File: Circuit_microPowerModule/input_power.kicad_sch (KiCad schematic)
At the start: 42 parts, among them Q2 MMBT3906, Q3 IRF5305S, Q4 RK7002BM, SW4 SW_SPDT, U7 MP2315S

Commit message: change licenses
updated some footprint, create nokia 5110 lcd module pcb symbol, updated reademe
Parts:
- D4: footprint (none) -> LED_SMD:LED_1206_3216Metric
- Q4: footprint (none) -> Package_TO_SOT_SMD:SOT-23-3
- R19, R20, R21, R22, R23, R24, R25, R26, R27, R28, R29, R30, R59, R60: footprint (none) -> Resistor_SMD:R_0603_1608Metric
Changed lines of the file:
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@@
       (effects (font (size 1.27 1.27)) (justify left))
     )
-    (property "Footprint" "" (at 241.3 43.434 0)
+    (property "Footprint" "Resistor_SMD:R_0603_1608Metric" (at 241.3 43.434 0)
       (effects (font (size 1.27 1.27)) hide)
     )
@@
       (effects (font (size 1.27 1.27)) (justify left))
     )
-    (property "Footprint" "" (at 68.58 43.434 0)
+    (property "Footprint" "Resistor_SMD:R_0603_1608Metric" (at 68.58 43.434 0)
       (effects (font (size 1.27 1.27)) hide)
     )
@@
       (effects (font (size 2.54 2.54) bold (color 255 0 0 1)) (justify left))
     )
-    (property "Footprint" "" (at 91.44 58.166 0)
+    (property "Footprint" "Resistor_SMD:R_0603_1608Metric" (at 91.44 58.166 0)
       (effects (font (size 1.27 1.27)) hide)
     )
@@
       (effects (font (size 1.27 1.27)))
     )
-    (property "Footprint" "" (at 205.232 66.04 0)
+    (property "Footprint" "Resistor_SMD:R_0603_1608Metric" (at 205.232 66.04 0)
       (effects (font (size 1.27 1.27)) hide)
     )
@@
       (effects (font (size 1.27 1.27)) (justify left))
     )
-    (property "Footprint" "" (at 144.78 43.18 0)
+    (property "Footprint" "Resistor_SMD:R_0603_1608Metric" (at 144.78 43.18 0)
       (effects (font (size 1.27 1.27)) hide)
     )
@@
       (effects (font (size 1.27 1.27)) (justify left))
     )
-    (property "Footprint" "" (at 144.78 67.818 0)
+    (property "Footprint" "Resistor_SMD:R_0603_1608Metric" (at 144.78 67.818 0)
       (effects (font (size 1.27 1.27)) hide)
     )
@@
       (effects (font (size 1.27 1.27)) (justify left))
     )
-    (property "Footprint" "" (at 116.84 70.104 0)
+    (property "Footprint" "Resistor_SMD:R_0603_1608Metric" (at 116.84 70.104 0)
       (effects (font (size 1.27 1.27)) hide)
     )
@@
       (effects (font (size 1.27 1.27)))
     )
-    (property "Footprint" "" (at 186.182 66.04 0)
+    (property "Footprint" "Resistor_SMD:R_0603_1608Metric" (at 186.182 66.04 0)
       (effects (font (size 1.27 1.27)) hide)
     )
@@
       (effects (font (size 1.27 1.27)) (justify left))
     )
-    (property "Footprint" "" (at 38.1 133.35 0)
+    (property "Footprint" "Resistor_SMD:R_0603_1608Metric" (at 38.1 133.35 0)
       (effects (font (size 1.27 1.27)) hide)
     )
@@
       (effects (font (size 1.27 1.27)))
     )
-    (property "Footprint" "" (at 172.72 68.58 0)
+    (property "Footprint" "Package_TO_SOT_SMD:SOT-23-3" (at 172.72 68.58 0)
       (effects (font (size 1.27 1.27)) hide)
     )
@@
       (effects (font (size 1.27 1.27)))
     )
-    (property "Footprint" "" (at 99.314 51.308 0)
+    (property "Footprint" "Resistor_SMD:R_0603_1608Metric" (at 99.314 51.308 0)
       (effects (font (size 1.27 1.27)) hide)
     )
@@
       (effects (font (size 1.27 1.27)) (justify left))
     )
-    (property "Footprint" "" (at 170.18 45.72 0)
+    (property "Footprint" "Resistor_SMD:R_0603_1608Metric" (at 170.18 45.72 0)
       (effects (font (size 1.27 1.27)) hide)
     )
@@
       (effects (font (size 1.27 1.27)) (justify left))
     )
-    (property "Footprint" "" (at 38.1 123.19 0)
+    (property "Footprint" "Resistor_SMD:R_0603_1608Metric" (at 38.1 123.19 0)
       (effects (font (size 1.27 1.27)) hide)
     )
@@
       (effects (font (size 1.27 1.27)) (justify right))
     )
-    (property "Footprint" "" (at 158.75 70.358 0)
+    (property "Footprint" "Resistor_SMD:R_0603_1608Metric" (at 158.75 70.358 0)
       (effects (font (size 1.27 1.27)) hide)
     )
@@
       (effects (font (size 1.27 1.27)) (justify left))
     )
-    (property "Footprint" "" (at 195.58 45.72 0)
+    (property "Footprint" "Resistor_SMD:R_0603_1608Metric" (at 195.58 45.72 0)
       (effects (font (size 1.27 1.27)) hide)
     )
@@
       (effects (font (size 1.27 1.27)) (justify right))
     )
-    (property "Footprint" "" (at 241.3 52.832 90)
-      (effects (font (size 1.27 1.27)) hide)
-    )
+    (property "Footprint" "LED_SMD:LED_1206_3216Metric" (at 241.3 52.832 90)
+      (effects (font (size 1.27 1.27)) hide)
+    )

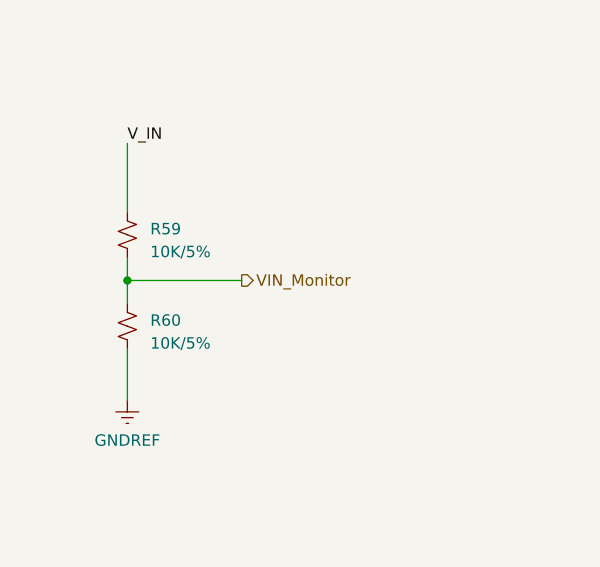
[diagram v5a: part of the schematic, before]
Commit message: update components footprint
check boost VR component, added Nokia 5110 LCD 3D module
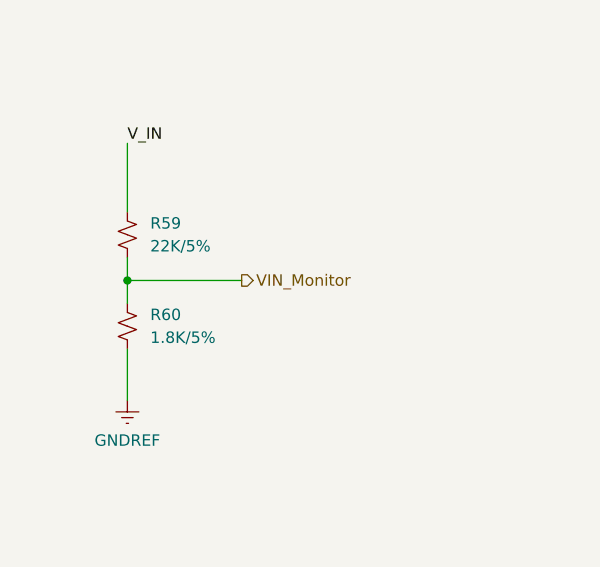
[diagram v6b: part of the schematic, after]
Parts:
- C1, C10, C11, C14, C2, C3, C6: footprint (none) -> Capacitor_SMD:C_0603_1608Metric
- D2, D3: footprint (none) -> Diode_SMD:D_SOD-123
- L1: footprint (none) -> Inductor_SMD_Wurth:L_Wurth_WE-LQSH-2512
- R59: value 10K/5% -> 22K/5%
- R60: value 10K/5% -> 1.8K/5%
- SW4: footprint (none) -> Button_Switch_THT:SW_Push_2P2T_Toggle_CK_PVA2xxH1xxxxxxV2
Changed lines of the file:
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@@
       (effects (font (size 1.27 1.27)) (justify left))
     )
-    (property "Footprint" "" (at 123.063 110.617 0)
+    (property "Footprint" "Capacitor_SMD:C_0603_1608Metric" (at 123.063 110.617 0)
       (effects (font (size 1.27 1.27)) hide)
     )
@@
       (effects (font (size 1.27 1.27)) (justify left))
     )
-    (property "Footprint" "" (at 152.019 118.872 0)
+    (property "Footprint" "Capacitor_SMD:C_0603_1608Metric" (at 152.019 118.872 0)
       (effects (font (size 1.27 1.27)) hide)
     )
@@
       (effects (font (size 1.27 1.27)) (justify left))
     )
-    (property "Footprint" "" (at 208.915 108.077 0)
+    (property "Footprint" "Capacitor_SMD:C_0603_1608Metric" (at 208.915 108.077 0)
       (effects (font (size 1.27 1.27)) hide)
     )
@@
       (effects (font (size 2.54 2.54) bold (color 255 0 0 1)))
     )
-    (property "Footprint" "" (at 204.47 55.88 90)
+    (property "Footprint" "Diode_SMD:D_SOD-123" (at 204.47 55.88 90)
       (effects (font (size 1.27 1.27)) hide)
     )
@@
       (effects (font (size 1.27 1.27)) (justify left))
     )
-    (property "Footprint" "" (at 217.805 124.333 0)
+    (property "Footprint" "Capacitor_SMD:C_0603_1608Metric" (at 217.805 124.333 0)
       (effects (font (size 1.27 1.27)) hide)
     )
@@
   (symbol (lib_id "Device:R_Small_US") (at 38.1 133.35 0) (unit 1)
     (in_bom yes) (on_board yes) (dnp no) (fields_autoplaced)
-    (property "Reference" "R60" (at 40.64 132.715 0)
-      (effects (font (size 1.27 1.27)) (justify left))
-    )
-    (property "Value" "10K/5%" (at 40.64 135.255 0)
+    (property "Reference" "R60" (at 40.64 132.08 0)
+      (effects (font (size 1.27 1.27)) (justify left))
+    )
+    (property "Value" "1.8K/5%" (at 40.64 134.62 0)
       (effects (font (size 1.27 1.27)) (justify left))
     )
@@
       (effects (font (size 1.27 1.27)) (justify left))
     )
-    (property "Footprint" "" (at 50.8 57.404 0)
+    (property "Footprint" "Capacitor_SMD:C_0603_1608Metric" (at 50.8 57.404 0)
       (effects (font (size 1.27 1.27)) hide)
     )
@@
       (effects (font (size 1.27 1.27)) (justify left))
     )
-    (property "Footprint" "" (at 213.36 45.72 0)
+    (property "Footprint" "Capacitor_SMD:C_0603_1608Metric" (at 213.36 45.72 0)
       (effects (font (size 1.27 1.27)) hide)
     )
@@
   (symbol (lib_id "Device:R_Small_US") (at 38.1 123.19 0) (unit 1)
     (in_bom yes) (on_board yes) (dnp no) (fields_autoplaced)
-    (property "Reference" "R59" (at 40.64 122.555 0)
-      (effects (font (size 1.27 1.27)) (justify left))
-    )
-    (property "Value" "10K/5%" (at 40.64 125.095 0)
+    (property "Reference" "R59" (at 40.64 121.92 0)
+      (effects (font (size 1.27 1.27)) (justify left))
+    )
+    (property "Value" "22K/5%" (at 40.64 124.46 0)
       (effects (font (size 1.27 1.27)) (justify left))
     )
@@
       (effects (font (size 1.27 1.27)) (justify left))
     )
-    (property "Footprint" "" (at 267.335 53.594 0)
+    (property "Footprint" "Capacitor_SMD:C_0603_1608Metric" (at 267.335 53.594 0)
       (effects (font (size 1.27 1.27)) hide)
     )
@@
       (effects (font (size 1.27 1.27)))
     )
-    (property "Footprint" "" (at 154.686 55.88 0)
+    (property "Footprint" "Button_Switch_THT:SW_Push_2P2T_Toggle_CK_PVA2xxH1xxxxxxV2" (at 154.686 55.88 0)
       (effects (font (size 1.27 1.27)) hide)
     )
@@
       (effects (font (size 1.27 1.27)))
     )
-    (property "Footprint" "" (at 216.281 111.125 0)
+    (property "Footprint" "Inductor_SMD_Wurth:L_Wurth_WE-LQSH-2512" (at 216.281 111.125 0)
       (effects (font (size 1.27 1.27)) hide)
     )
@@
       (effects (font (size 1.27 1.27)) (justify right))
     )
-    (property "Footprint" "" (at 68.58 58.166 90)
-      (effects (font (size 1.27 1.27)) hide)
-    )
-    (property "Datasheet" "~" (at 68.58 58.166 90)
-      (effects (font (size 1.27 1.27)) hide)
-    )
+    (property "Footprint" "Diode_SMD:D_SOD-123" (at 68.58 58.166 90)
+      (effects (font (size 1.27 1.27)) hide)
+    )
+    (property "Datasheet" "https://www.diodes.com/assets/Datasheets/ds18004.pdf" (at 68.58 58.166 90)
+      (effects (font (size 1.27 1.27)) hide)
+    )

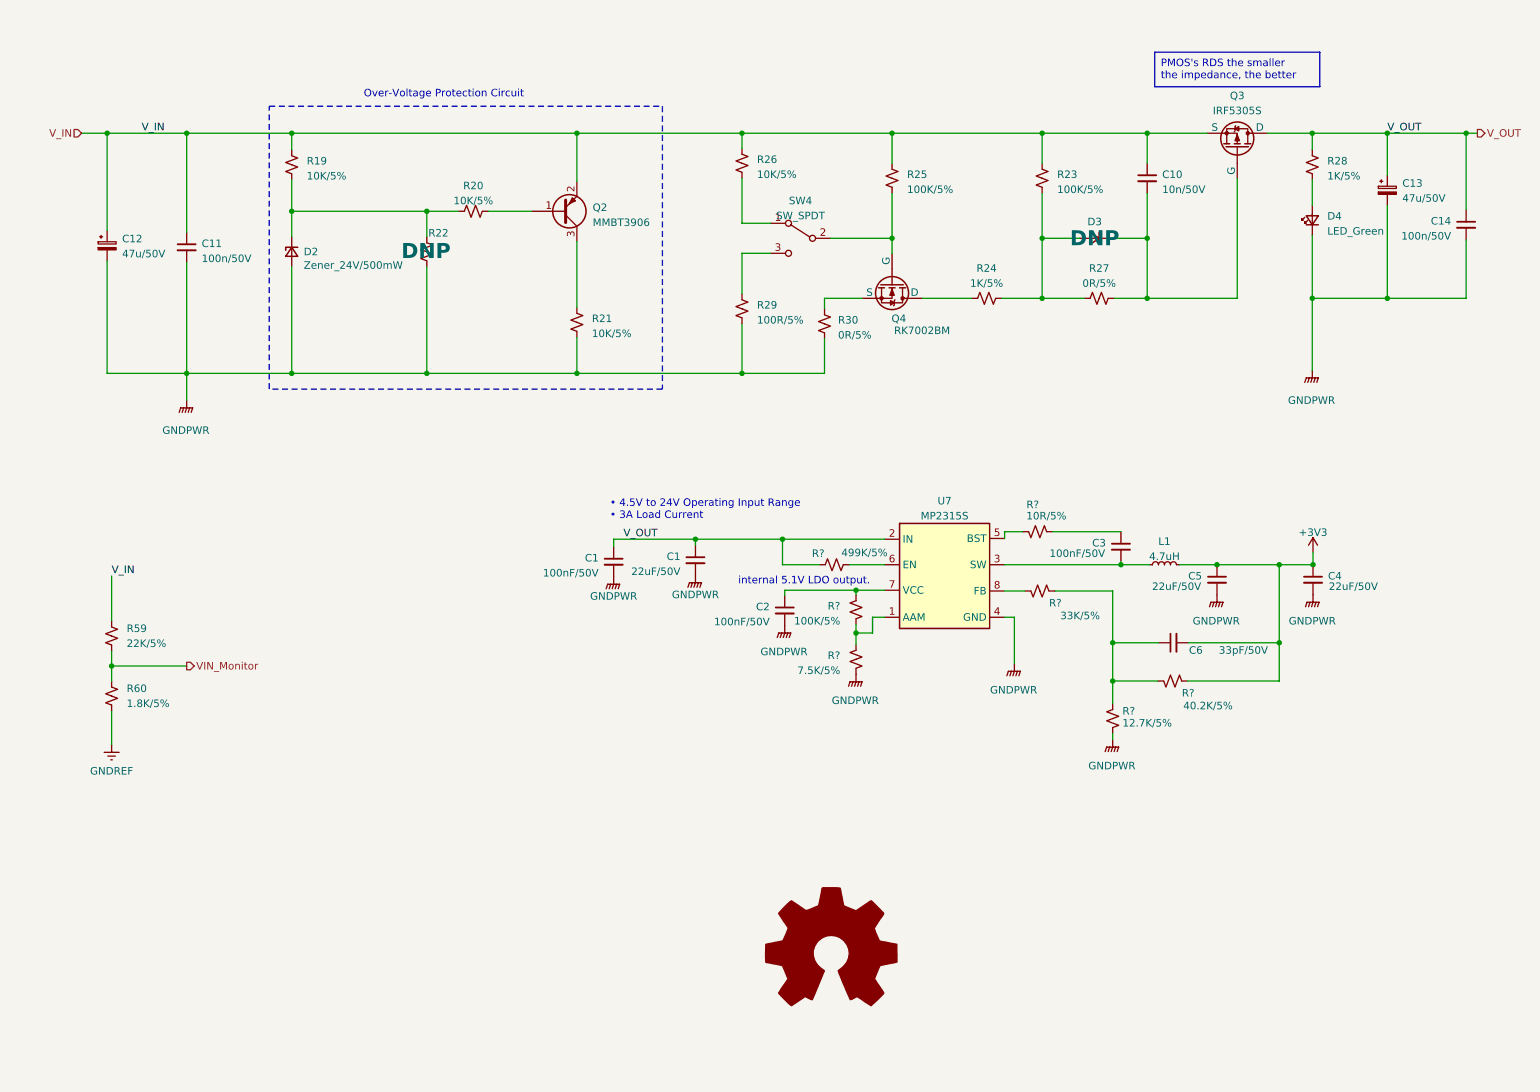
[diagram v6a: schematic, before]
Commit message: update schematic
added pin assessment to readme
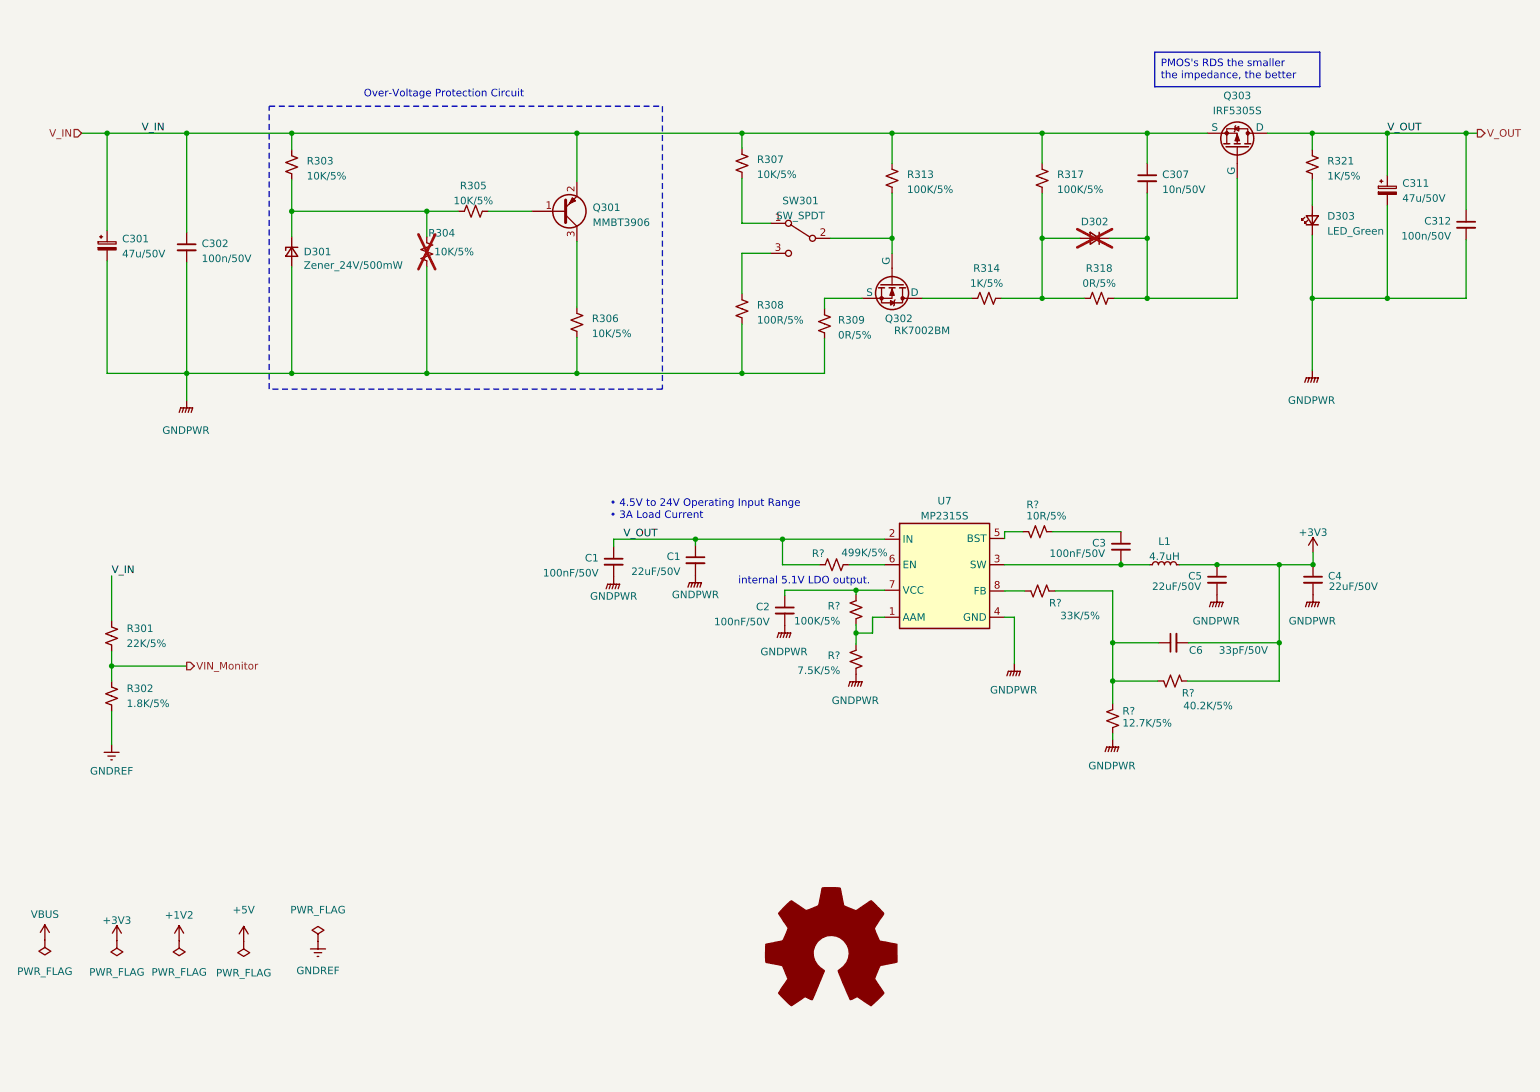
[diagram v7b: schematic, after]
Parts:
- D302: renamed from D3; now not fitted
- R304: renamed from R22; value DNP -> 10K/5%; now not fitted
- renumbered C12 to C301, C11 to C302, C10 to C307, C13 to C311, C14 to C312, D2 to D301, D4 to D303, Q2 to Q301, Q4 to Q302, Q3 to Q303, R59 to R301, R60 to R302, R19 to R303, R20 to R305, R21 to R306, R26 to R307, R29 to R308, R30 to R309, R25 to R313, R24 to R314, R23 to R317, R27 to R318, R28 to R321, SW4 to SW301

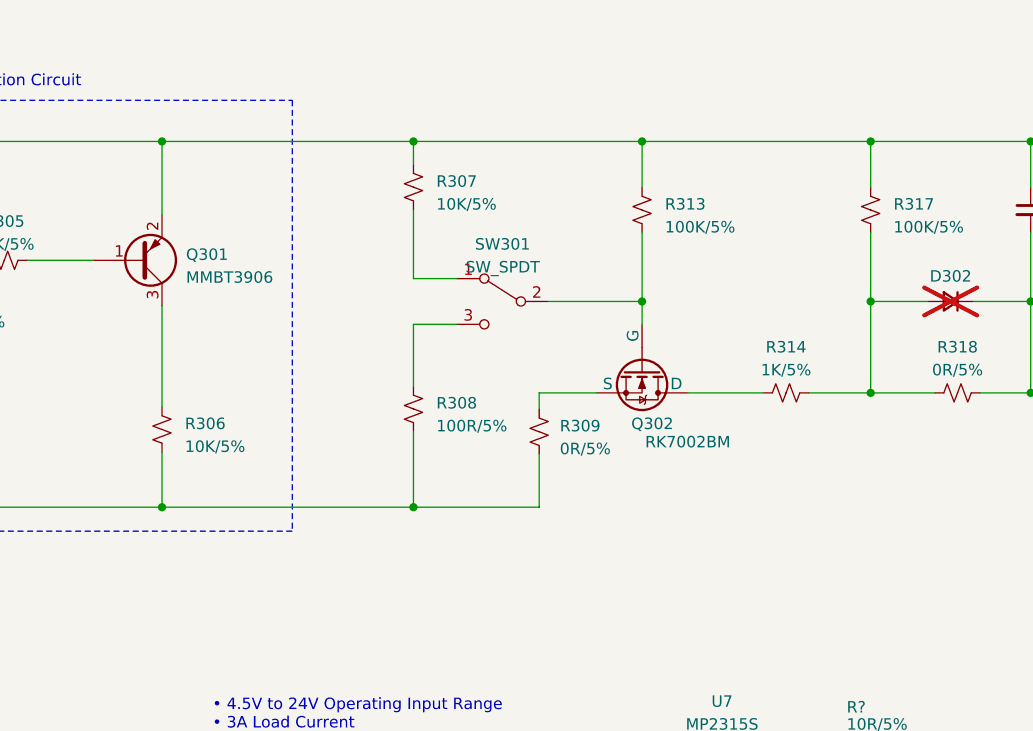
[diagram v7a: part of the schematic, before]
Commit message: added H-Bridge
Control load forward or reverse (current direction)
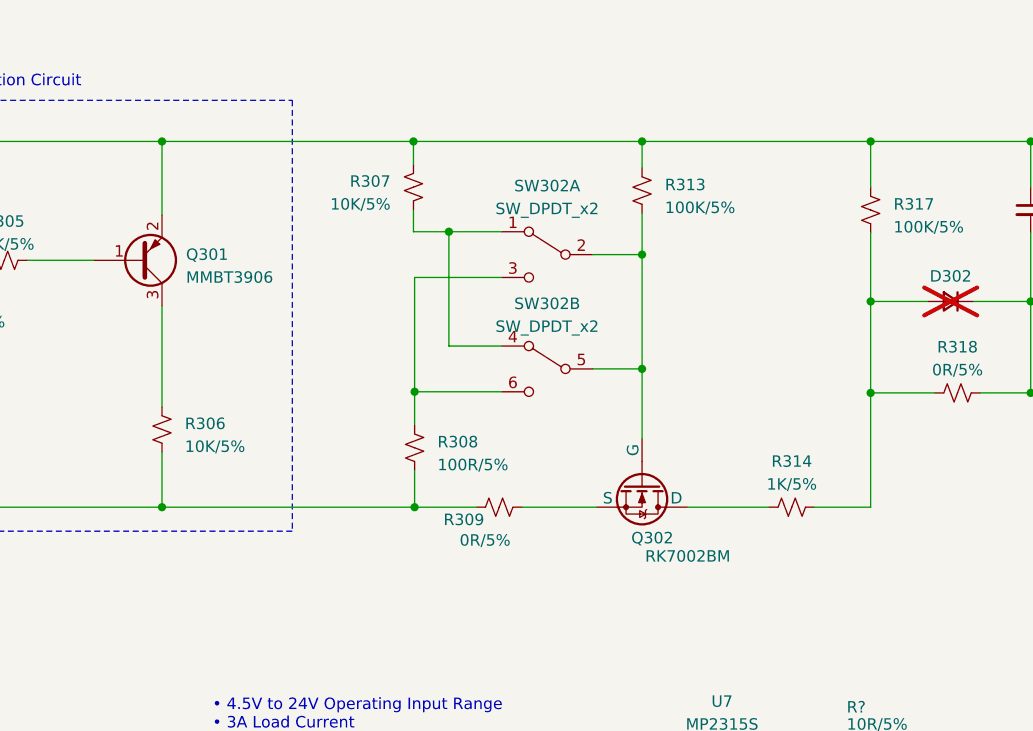
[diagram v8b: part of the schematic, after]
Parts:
- removed SW301: SW_SPDT, Button_Switch_THT:SW_Push_2P2T_Toggle_CK_PVA2xxH1xxxxxxV2, symbol Switch:SW_SPDT
- added SW302: SW_DPDT_x2, Button_Switch_THT:SW_Push_2P2T_Toggle_CK_PVA2xxH1xxxxxxV2, symbol Switch:SW_DPDT_x2
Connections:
- net GNDPWR: now also R309.2; no longer R309.1
- net at R307.2: now also SW302.1 (A), SW302.4 (A)
- net at R308.1: now also SW302.3 (C), SW302.6 (C)
- net at Q302.2 (G), R313.2: now also SW302.2 (B), SW302.5 (B)
- net at Q302.3 (S): now also R309.1; no longer R309.2
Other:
- moved on the sheet: Q302, R308, R309, R313, R314
